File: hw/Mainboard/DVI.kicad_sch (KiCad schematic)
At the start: 16 parts, among them J23 NOT_HDMI_A

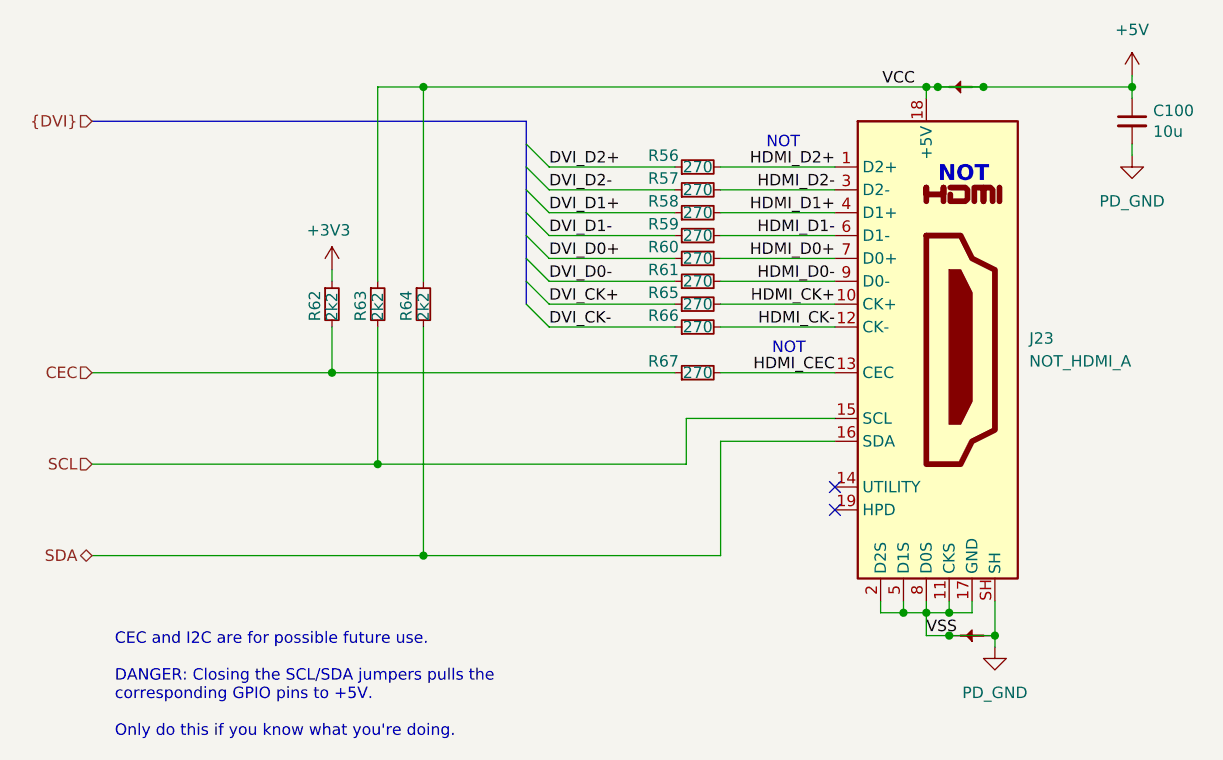
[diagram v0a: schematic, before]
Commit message: hw: remove net/power ties
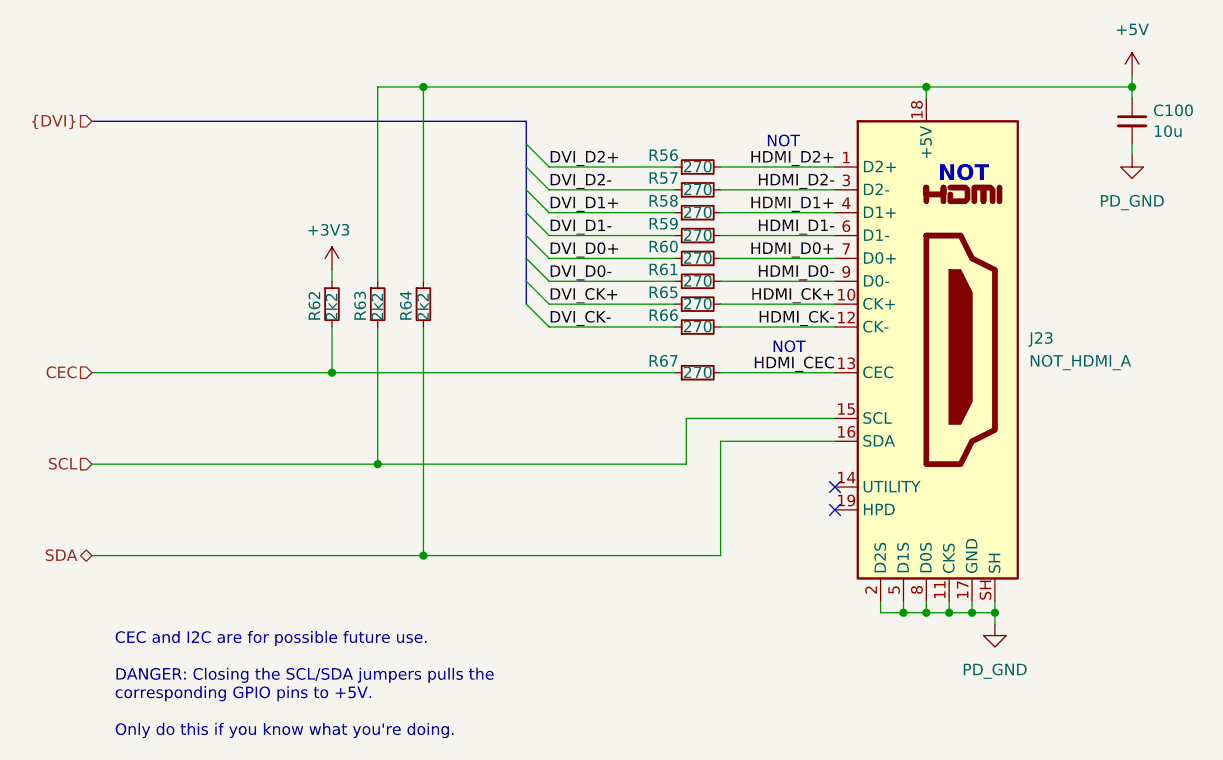
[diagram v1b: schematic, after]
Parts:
- removed PT49, PT50: PowerTie_2, PET:NetTie-2_SMD_Pad_1.6_to_0.4mm, symbol PET:PowerTie_2
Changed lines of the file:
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@@
   (junction (at 134.62 111.76) (diameter 0) (color 0 0 0 0)
   )
-  (junction (at 196.85 59.69) (diameter 0) (color 0 0 0 0)
-  )
-  (junction (at 193.04 120.65) (diameter 0) (color 0 0 0 0)
-  )
   (junction (at 213.36 59.69) (diameter 0) (color 0 0 0 0)
   )
@@
   (junction (at 190.5 59.69) (diameter 0) (color 0 0 0 0)
   )
-  (junction (at 191.77 59.69) (diameter 0) (color 0 0 0 0)
-  )
   (junction (at 134.62 59.69) (diameter 0) (color 0 0 0 0)
   )
-  (junction (at 198.12 120.65) (diameter 0) (color 0 0 0 0)
-  )
   (junction (at 190.5 118.11) (diameter 0) (color 0 0 0 0)
   )
   (junction (at 129.54 101.6) (diameter 0) (color 0 0 0 0)
   )
+  (junction (at 198.12 118.11) (diameter 0) (color 0 0 0 0)
+  )
   (junction (at 187.96 118.11) (diameter 0) (color 0 0 0 0)
   )
   (junction (at 124.46 91.44) (diameter 0) (color 0 0 0 0)
+  )
+  (junction (at 195.58 118.11) (diameter 0) (color 0 0 0 0)
   )
   (no_connect (at 180.34 104.14))
@@
     (stroke (width 0) (type default) (color 0 0 0 0))
   )
-  (wire (pts (xy 190.5 118.11) (xy 190.5 120.65))
-    (stroke (width 0) (type default) (color 0 0 0 0))
-  )
   (wire (pts (xy 167.64 111.76) (xy 167.64 99.06))
     (stroke (width 0) (type default) (color 0 0 0 0))
@@
     (stroke (width 0) (type default) (color 0 0 0 0))
   )
-  (wire (pts (xy 196.85 59.69) (xy 213.36 59.69))
+  (wire (pts (xy 190.5 59.69) (xy 213.36 59.69))
     (stroke (width 0) (type default) (color 0 0 0 0))
   )
@@
     (stroke (width 0) (type default) (color 0 0 0 0))
   )
-  (wire (pts (xy 191.77 59.69) (xy 190.5 59.69))
-    (stroke (width 0) (type default) (color 0 0 0 0))
-  )
   (wire (pts (xy 134.62 59.69) (xy 134.62 81.28))
     (stroke (width 0) (type default) (color 0 0 0 0))
@@
     (stroke (width 0) (type default) (color 0 0 0 0))
   )
-  (wire (pts (xy 198.12 116.84) (xy 198.12 120.65))
+  (wire (pts (xy 195.58 118.11) (xy 198.12 118.11))
+    (stroke (width 0) (type default) (color 0 0 0 0))
+  )
+  (wire (pts (xy 198.12 116.84) (xy 198.12 118.11))
     (stroke (width 0) (type default) (color 0 0 0 0))
   )
@@
     (stroke (width 0) (type default) (color 0 0 0 0))
   )
+  (wire (pts (xy 198.12 118.11) (xy 198.12 119.38))
+    (stroke (width 0) (type default) (color 0 0 0 0))
+  )
   (wire (pts (xy 190.5 116.84) (xy 190.5 118.11))
     (stroke (width 0) (type default) (color 0 0 0 0))
   )
-  (wire (pts (xy 190.5 120.65) (xy 193.04 120.65))
-    (stroke (width 0) (type default) (color 0 0 0 0))
-  )
   (wire (pts (xy 187.96 118.11) (xy 190.5 118.11))
     (stroke (width 0) (type default) (color 0 0 0 0))
@@
     (stroke (width 0) (type default) (color 0 0 0 0))
   )
-  (wire (pts (xy 198.12 120.65) (xy 198.12 121.92))
-    (stroke (width 0) (type default) (color 0 0 0 0))
-  )
   (wire (pts (xy 193.04 118.11) (xy 195.58 118.11))
     (stroke (width 0) (type default) (color 0 0 0 0))
@@
   )
   (wire (pts (xy 213.36 60.96) (xy 213.36 59.69))
-    (stroke (width 0) (type default) (color 0 0 0 0))
-  )
-  (wire (pts (xy 191.77 59.69) (xy 196.85 59.69))
-    (stroke (width 0) (type default) (color 0 0 0 0))
-  )
-  (wire (pts (xy 193.04 120.65) (xy 198.12 120.65))
     (stroke (width 0) (type default) (color 0 0 0 0))
   )
@@
     (effects (font (size 1.27 1.27)) (justify right bottom))
   )
-  (label "VSS" (at 190.5 120.65 0)
-    (effects (font (size 1.27 1.27)) (justify left bottom))
-  )
   (label "HDMI_CK+" (at 180.34 83.82 180)
     (effects (font (size 1.27 1.27)) (justify right bottom))
@@
   )
   (label "HDMI_D1-" (at 180.34 76.2 180)
-    (effects (font (size 1.27 1.27)) (justify right bottom))
-  )
-  (label "VCC" (at 189.23 59.69 180)
     (effects (font (size 1.27 1.27)) (justify right bottom))
   )
@@
     (pin "2")
   )
-  (symbol (lib_id "PET:PowerTie_2") (at 195.58 120.65 180) (unit 1)
-    (in_bom yes) (on_board yes) (fields_autoplaced)
-    (property "Reference" "PT50" (id 0) (at 195.58 122.555 0)
-      (effects (font (size 1.27 1.27)) hide)
-    )
-    (property "Value" "PowerTie_2" (id 1) (at 195.58 118.745 0)
-      (effects (font (size 1.27 1.27)) hide)
-    )
-    (property "Footprint" "PET:NetTie-2_SMD_Pad_1.6_to_0.4mm" (id 2) (at 195.58 120.65 0)
-      (effects (font (size 1.27 1.27)) hide)
-    )
-    (property "Datasheet" "~" (id 3) (at 195.58 120.65 0)
-      (effects (font (size 1.27 1.27)) hide)
-    )
-    (pin "1")
-    (pin "2")
-  )
   (symbol (lib_id "Device:R_Small") (at 129.54 83.82 0) (unit 1)
     (in_bom yes) (on_board yes)
@@
     )
     (pin "1")
-  )
-  (symbol (lib_id "PET:PowerTie_2") (at 194.31 59.69 180) (unit 1)
-    (in_bom yes) (on_board yes) (fields_autoplaced)
-    (property "Reference" "PT49" (id 0) (at 194.31 61.595 0)
-      (effects (font (size 1.27 1.27)) hide)
-    )
-    (property "Value" "PowerTie_2" (id 1) (at 194.31 57.785 0)
-      (effects (font (size 1.27 1.27)) hide)
-    )
-    (property "Footprint" "PET:NetTie-2_SMD_Pad_1.6_to_0.4mm" (id 2) (at 194.31 59.69 0)
-      (effects (font (size 1.27 1.27)) hide)
-    )
-    (property "Datasheet" "~" (id 3) (at 194.31 59.69 0)
-      (effects (font (size 1.27 1.27)) hide)
-    )
-    (pin "1")
-    (pin "2")
   )
   (symbol (lib_id "power:+3V3") (at 124.46 80.01 0) (mirror y) (unit 1)
@@
     (pin "2")
   )
-  (symbol (lib_id "PET:PD_GND") (at 198.12 121.92 0) (unit 1)
+  (symbol (lib_id "PET:PD_GND") (at 198.12 119.38 0) (unit 1)
     (in_bom yes) (on_board yes) (fields_autoplaced)
-    (property "Reference" "#PWR0151" (id 0) (at 198.12 128.27 0)
-      (effects (font (size 1.27 1.27)) hide)
-    )
-    (property "Value" "PD_GND" (id 1) (at 198.12 127 0))
-    (property "Footprint" "" (id 2) (at 198.12 121.92 0)
-      (effects (font (size 1.27 1.27)) hide)
-    )
-    (property "Datasheet" "" (id 3) (at 198.12 121.92 0)
-      (effects (font (size 1.27 1.27)) hide)
-    )
+    (property "Reference" "#PWR0151" (id 0) (at 198.12 125.73 0)
+      (effects (font (size 1.27 1.27)) hide)
+    )
+    (property "Value" "PD_GND" (id 1) (at 198.12 124.46 0))
+    (property "Footprint" "" (id 2) (at 198.12 119.38 0)
+      (effects (font (size 1.27 1.27)) hide)
+    )
+    (property "Datasheet" "" (id 3) (at 198.12 119.38 0)
+      (effects (font (size 1.27 1.27)) hide)
+    )

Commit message: hw: renumber J* refs to match PET connectors
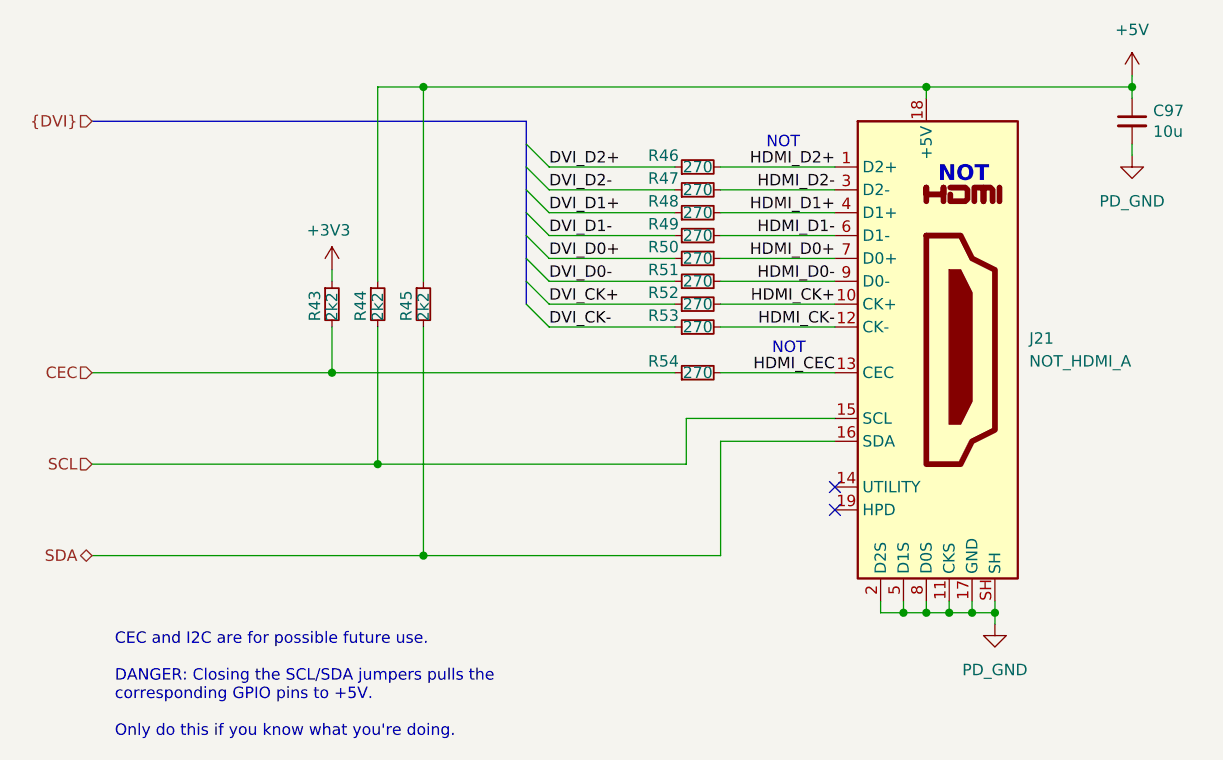
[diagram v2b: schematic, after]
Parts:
- renumbered C100 to C97, J23 to J21, R62 to R43, R63 to R44, R64 to R45, R56 to R46, R57 to R47, R58 to R48, R59 to R49, R60 to R50, R61 to R51, R65 to R52, R66 to R53, R67 to R54
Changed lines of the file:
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@@
   (symbol (lib_id "Device:R_Small") (at 165.1 83.82 90) (unit 1)
     (in_bom yes) (on_board yes)
-    (property "Reference" "R65" (id 0) (at 161.29 82.55 90))
+    (property "Reference" "R52" (id 0) (at 161.29 82.55 90))
     (property "Value" "270" (id 1) (at 165.1 83.82 90))
     (property "Footprint" "Resistor_SMD:R_0603_1608Metric" (id 2) (at 165.1 83.82 0)
@@
   (symbol (lib_id "Device:R_Small") (at 165.1 76.2 90) (unit 1)
     (in_bom yes) (on_board yes)
-    (property "Reference" "R59" (id 0) (at 161.29 74.93 90))
+    (property "Reference" "R49" (id 0) (at 161.29 74.93 90))
     (property "Value" "270" (id 1) (at 165.1 76.2 90))
     (property "Footprint" "Resistor_SMD:R_0603_1608Metric" (id 2) (at 165.1 76.2 0)
@@
   (symbol (lib_id "Device:R_Small") (at 134.62 83.82 0) (unit 1)
     (in_bom yes) (on_board yes)
-    (property "Reference" "R64" (id 0) (at 132.715 85.725 90)
+    (property "Reference" "R45" (id 0) (at 132.715 85.725 90)
       (effects (font (size 1.27 1.27)) (justify left))
     )
@@
   (symbol (lib_id "Device:R_Small") (at 129.54 83.82 0) (unit 1)
     (in_bom yes) (on_board yes)
-    (property "Reference" "R63" (id 0) (at 127.635 85.725 90)
+    (property "Reference" "R44" (id 0) (at 127.635 85.725 90)
       (effects (font (size 1.27 1.27)) (justify left))
     )
@@
   (symbol (lib_id "power:+5V") (at 213.36 58.42 0) (unit 1)
     (in_bom yes) (on_board yes) (fields_autoplaced)
-    (property "Reference" "#PWR0149" (id 0) (at 213.36 62.23 0)
+    (property "Reference" "#PWR0163" (id 0) (at 213.36 62.23 0)
       (effects (font (size 1.27 1.27)) hide)
     )
@@
   (symbol (lib_id "power:+3V3") (at 124.46 80.01 0) (mirror y) (unit 1)
     (in_bom yes) (on_board yes)
-    (property "Reference" "#PWR0150" (id 0) (at 124.46 83.82 0)
+    (property "Reference" "#PWR0161" (id 0) (at 124.46 83.82 0)
       (effects (font (size 1.27 1.27)) hide)
     )
@@
   (symbol (lib_id "Connector:HDMI_A") (at 190.5 88.9 0) (unit 1)
     (in_bom yes) (on_board yes)
-    (property "Reference" "J23" (id 0) (at 201.93 87.63 0)
+    (property "Reference" "J21" (id 0) (at 201.93 87.63 0)
       (effects (font (size 1.27 1.27)) (justify left))
     )
@@
   (symbol (lib_id "Device:R_Small") (at 165.1 68.58 90) (unit 1)
     (in_bom yes) (on_board yes)
-    (property "Reference" "R56" (id 0) (at 161.29 67.31 90))
+    (property "Reference" "R46" (id 0) (at 161.29 67.31 90))
     (property "Value" "270" (id 1) (at 165.1 68.58 90))
     (property "Footprint" "Resistor_SMD:R_0603_1608Metric" (id 2) (at 165.1 68.58 0)
@@
   (symbol (lib_id "Device:R_Small") (at 165.1 91.44 90) (unit 1)
     (in_bom yes) (on_board yes)
-    (property "Reference" "R67" (id 0) (at 161.29 90.17 90))
+    (property "Reference" "R54" (id 0) (at 161.29 90.17 90))
     (property "Value" "270" (id 1) (at 165.1 91.44 90))
     (property "Footprint" "Resistor_SMD:R_0603_1608Metric" (id 2) (at 165.1 91.44 0)
@@
   (symbol (lib_id "Device:R_Small") (at 165.1 81.28 90) (unit 1)
     (in_bom yes) (on_board yes)
-    (property "Reference" "R61" (id 0) (at 161.29 80.01 90))
+    (property "Reference" "R51" (id 0) (at 161.29 80.01 90))
     (property "Value" "270" (id 1) (at 165.1 81.28 90))
     (property "Footprint" "Resistor_SMD:R_0603_1608Metric" (id 2) (at 165.1 81.28 0)
@@
   (symbol (lib_id "Device:R_Small") (at 165.1 86.36 90) (unit 1)
     (in_bom yes) (on_board yes)
-    (property "Reference" "R66" (id 0) (at 161.29 85.09 90))
+    (property "Reference" "R53" (id 0) (at 161.29 85.09 90))
     (property "Value" "270" (id 1) (at 165.1 86.36 90))
     (property "Footprint" "Resistor_SMD:R_0603_1608Metric" (id 2) (at 165.1 86.36 0)
@@
   (symbol (lib_id "Device:C_Small") (at 213.36 63.5 0) (unit 1)
     (in_bom yes) (on_board yes)
-    (property "Reference" "C100" (id 0) (at 215.6968 62.3316 0)
+    (property "Reference" "C97" (id 0) (at 215.6968 62.3316 0)
       (effects (font (size 1.27 1.27)) (justify left))
     )
@@
   (symbol (lib_id "Device:R_Small") (at 165.1 78.74 90) (unit 1)
     (in_bom yes) (on_board yes)
-    (property "Reference" "R60" (id 0) (at 161.29 77.47 90))
+    (property "Reference" "R50" (id 0) (at 161.29 77.47 90))
     (property "Value" "270" (id 1) (at 165.1 78.74 90))
     (property "Footprint" "Resistor_SMD:R_0603_1608Metric" (id 2) (at 165.1 78.74 0)
@@
   (symbol (lib_id "Device:R_Small") (at 124.46 83.82 0) (unit 1)
     (in_bom yes) (on_board yes)
-    (property "Reference" "R62" (id 0) (at 122.555 85.725 90)
+    (property "Reference" "R43" (id 0) (at 122.555 85.725 90)
       (effects (font (size 1.27 1.27)) (justify left))
     )
@@
   (symbol (lib_id "PET:PD_GND") (at 198.12 119.38 0) (unit 1)
     (in_bom yes) (on_board yes) (fields_autoplaced)
-    (property "Reference" "#PWR0151" (id 0) (at 198.12 125.73 0)
+    (property "Reference" "#PWR0162" (id 0) (at 198.12 125.73 0)
       (effects (font (size 1.27 1.27)) hide)
     )
@@
   (symbol (lib_id "Device:R_Small") (at 165.1 71.12 90) (unit 1)
     (in_bom yes) (on_board yes)
-    (property "Reference" "R57" (id 0) (at 161.29 69.85 90))
+    (property "Reference" "R47" (id 0) (at 161.29 69.85 90))
     (property "Value" "270" (id 1) (at 165.1 71.12 90))
     (property "Footprint" "Resistor_SMD:R_0603_1608Metric" (id 2) (at 165.1 71.12 0)
@@
   (symbol (lib_id "Device:R_Small") (at 165.1 73.66 90) (unit 1)
     (in_bom yes) (on_board yes)
-    (property "Reference" "R58" (id 0) (at 161.29 72.39 90))
+    (property "Reference" "R48" (id 0) (at 161.29 72.39 90))
     (property "Value" "270" (id 1) (at 165.1 73.66 90))
     (property "Footprint" "Resistor_SMD:R_0603_1608Metric" (id 2) (at 165.1 73.66 0)
@@
   (symbol (lib_id "PET:PD_GND") (at 213.36 67.31 0) (unit 1)
     (in_bom yes) (on_board yes) (fields_autoplaced)
-    (property "Reference" "#PWR0176" (id 0) (at 213.36 73.66 0)
-      (effects (font (size 1.27 1.27)) hide)
-    )
+    (property "Reference" "#PWR0164" (id 0) (at 213.36 73.66 0)
+      (effects (font (size 1.27 1.27)) hide)
+    )
